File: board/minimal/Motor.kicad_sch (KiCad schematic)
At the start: 12 parts, among them IC1 DRV8835DSSR, J3 FR_ESC, J4 FL_ESC, J5 RMotor, J6 LMotor, J7 RR_ESC, J8 RL_ESC, Q1 DMP6050SSD

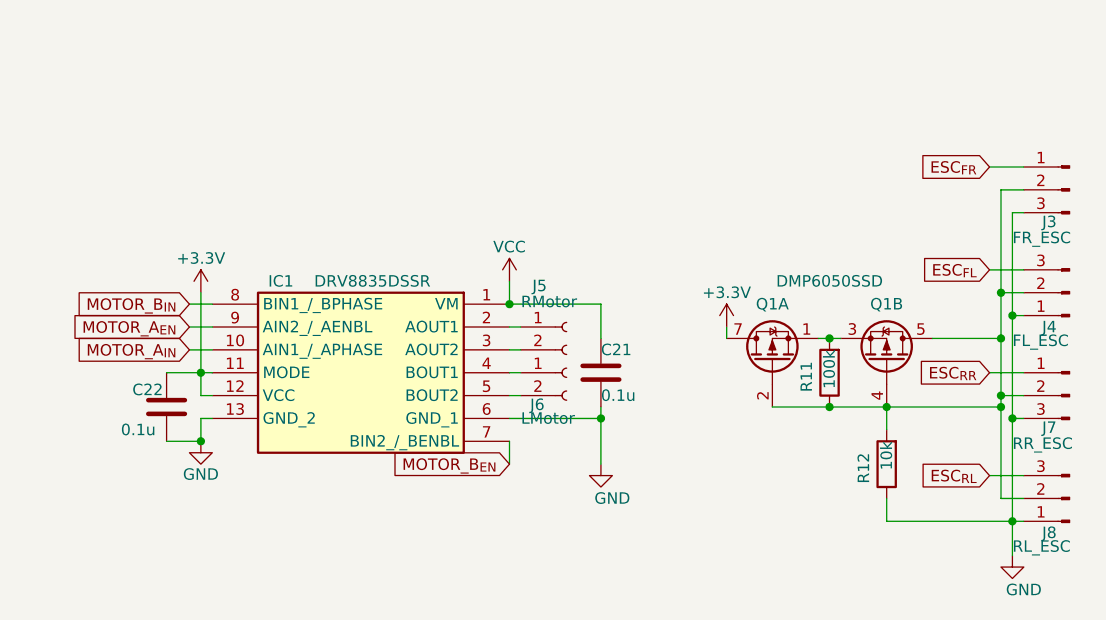
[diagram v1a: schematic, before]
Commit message: change core to rp2350b and some pin out
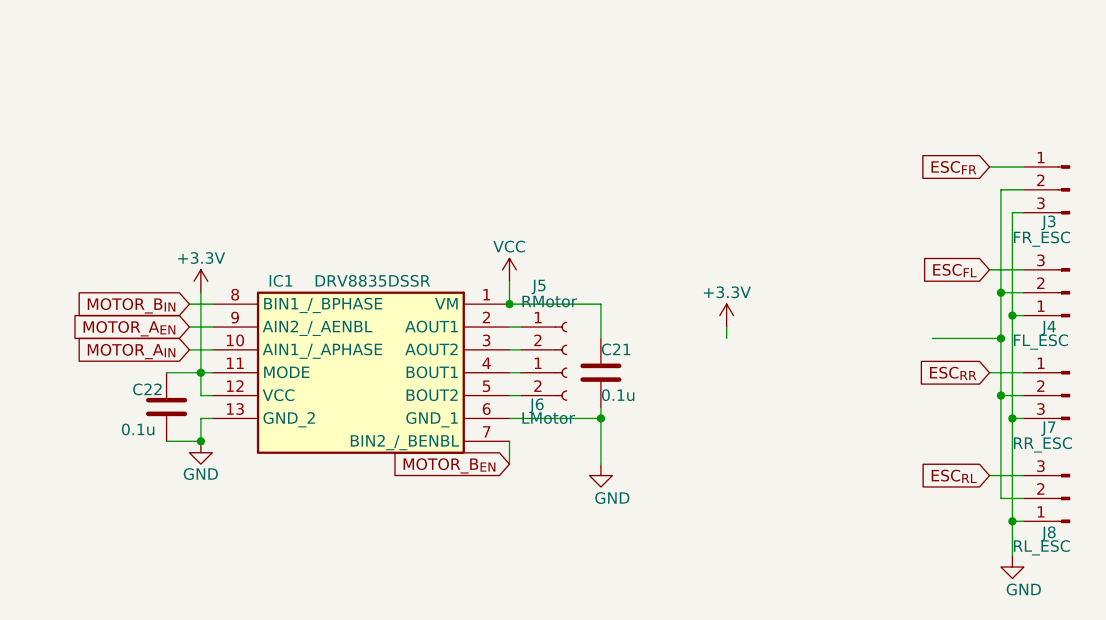
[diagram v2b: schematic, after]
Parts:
- removed Q1: DMP6050SSD, Package_SO:SOIC-8_3.9x4.9mm_P1.27mm, symbol Transistor_FET:DMP6050SSD
- removed R11: 100k, Resistor_SMD:R_0603_1608Metric, symbol Device:R
- removed R12: 10k, Resistor_SMD:R_0603_1608Metric, symbol Device:R

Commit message: add some connectors
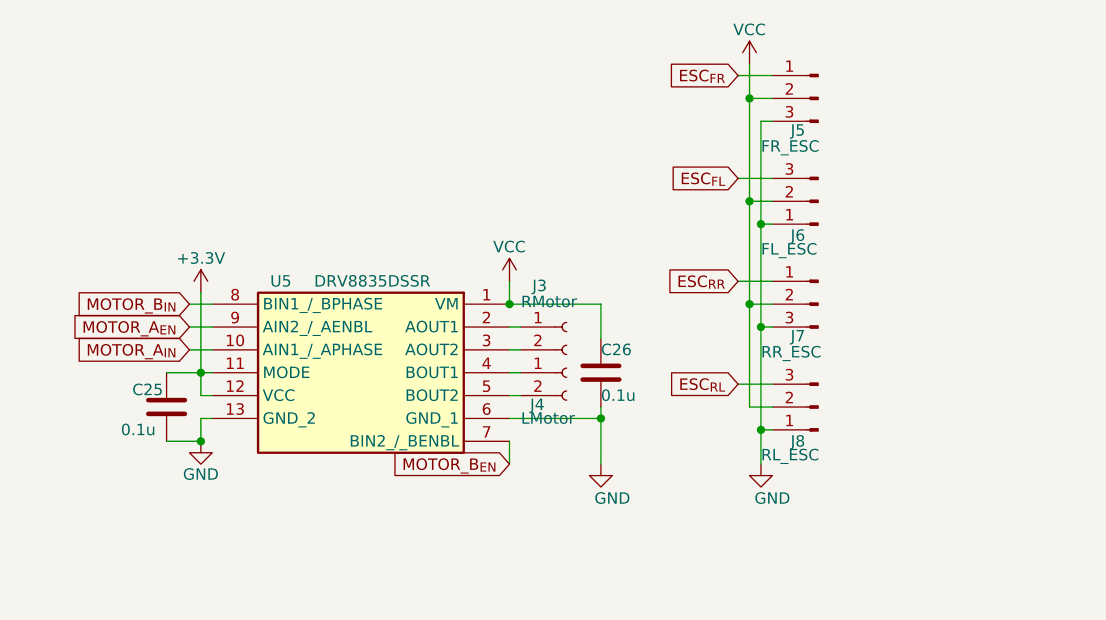
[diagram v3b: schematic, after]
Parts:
- renumbered C22 to C25, C21 to C26, J5 to J3, J6 to J4, J3 to J5, J4 to J6, IC1 to U5
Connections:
- net VCC: now also J5.2 (Pin_2), J6.2 (Pin_2), J7.2 (Pin_2), J8.2 (Pin_2)
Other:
- moved on the sheet: J5, J6, J7, J8

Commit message: set footprint
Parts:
- renumbered C25 to C26, C26 to C27, J3 to J4, J4 to J5, J5 to J6, J6 to J7, J7 to J8, J8 to J9
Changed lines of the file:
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@@
 		(on_board yes)
 		(dnp no)
-		(property "Reference" "#PWR032"
+		(property "Reference" "#PWR038"
 			(at 140.97 100.33 0)
 			(hide yes)
@@
 			(project "TurtlePico-Minimal"
 				(path "/7af2d99d-e350-48e7-86b4-20911ea922f3/30a58c44-3c8a-4ad6-a7be-85fee873ce7a"
-					(reference "#PWR032")
+					(reference "#PWR038")
 					(unit 1)
 				)
@@
 		(on_board yes)
 		(dnp no)
-		(property "Reference" "#PWR033"
+		(property "Reference" "#PWR039"
 			(at 151.13 123.19 0)
 			(hide yes)
@@
 			(project "TurtlePico-Minimal"
 				(path "/7af2d99d-e350-48e7-86b4-20911ea922f3/30a58c44-3c8a-4ad6-a7be-85fee873ce7a"
-					(reference "#PWR033")
+					(reference "#PWR039")
 					(unit 1)
 				)
@@
 		(on_board yes)
 		(dnp no)
-		(property "Reference" "#PWR031"
+		(property "Reference" "#PWR037"
 			(at 106.68 120.65 0)
 			(hide yes)
@@
 			(project "TurtlePico-Minimal"
 				(path "/7af2d99d-e350-48e7-86b4-20911ea922f3/30a58c44-3c8a-4ad6-a7be-85fee873ce7a"
-					(reference "#PWR031")
+					(reference "#PWR037")
 					(unit 1)
 				)
@@
 		(on_board yes)
 		(dnp no)
-		(property "Reference" "#PWR030"
+		(property "Reference" "#PWR036"
 			(at 106.68 101.6 0)
 			(hide yes)
@@
 			(project "TurtlePico-Minimal"
 				(path "/7af2d99d-e350-48e7-86b4-20911ea922f3/30a58c44-3c8a-4ad6-a7be-85fee873ce7a"
-					(reference "#PWR030")
+					(reference "#PWR036")
 					(unit 1)
 				)
@@
 		(on_board yes)
 		(dnp no)
-		(property "Reference" "C26"
+		(property "Reference" "C27"
 			(at 151.13 104.14 0)
 			(effects
@@
 			(project "TurtlePico-Minimal"
 				(path "/7af2d99d-e350-48e7-86b4-20911ea922f3/30a58c44-3c8a-4ad6-a7be-85fee873ce7a"
-					(reference "C26")
+					(reference "C27")
 					(unit 1)
 				)
@@
 		(on_board yes)
 		(dnp no)
-		(property "Reference" "C25"
+		(property "Reference" "C26"
 			(at 99.06 108.585 0)
 			(effects
@@
 			(project "TurtlePico-Minimal"
 				(path "/7af2d99d-e350-48e7-86b4-20911ea922f3/30a58c44-3c8a-4ad6-a7be-85fee873ce7a"
-					(reference "C25")
+					(reference "C26")
 					(unit 1)
 				)
@@
 		(on_board yes)
 		(dnp no)
-		(property "Reference" "J6"
+		(property "Reference" "J7"
 			(at 172.212 91.44 0)
 			(effects
@@
 			(project "TurtlePico-Minimal"
 				(path "/7af2d99d-e350-48e7-86b4-20911ea922f3/30a58c44-3c8a-4ad6-a7be-85fee873ce7a"
-					(reference "J6")
+					(reference "J7")
 					(unit 1)
 				)
@@
 		(on_board yes)
 		(dnp no)
-		(property "Reference" "#PWR035"
+		(property "Reference" "#PWR041"
 			(at 168.91 123.19 0)
 			(hide yes)
@@
 			(project "TurtlePico-Minimal"
 				(path "/7af2d99d-e350-48e7-86b4-20911ea922f3/30a58c44-3c8a-4ad6-a7be-85fee873ce7a"
-					(reference "#PWR035")
+					(reference "#PWR041")
 					(unit 1)
 				)
@@
 		(on_board yes)
 		(dnp no)
-		(property "Reference" "#PWR034"
+		(property "Reference" "#PWR040"
 			(at 167.64 76.2 0)
 			(hide yes)
@@
 			(project "TurtlePico-Minimal"
 				(path "/7af2d99d-e350-48e7-86b4-20911ea922f3/30a58c44-3c8a-4ad6-a7be-85fee873ce7a"
-					(reference "#PWR034")
+					(reference "#PWR040")
 					(unit 1)
 				)
@@
 		(on_board yes)
 		(dnp no)
-		(property "Reference" "J4"
+		(property "Reference" "J5"
 			(at 143.256 110.236 0)
 			(effects
@@
 			(project "TurtlePico-Minimal"
 				(path "/7af2d99d-e350-48e7-86b4-20911ea922f3/30a58c44-3c8a-4ad6-a7be-85fee873ce7a"
-					(reference "J4")
+					(reference "J5")
 					(unit 1)
 				)
@@
 		(on_board yes)
 		(dnp no)
-		(property "Reference" "J3"
+		(property "Reference" "J4"
 			(at 143.51 97.028 0)
 			(effects
@@
 			(project "TurtlePico-Minimal"
 				(path "/7af2d99d-e350-48e7-86b4-20911ea922f3/30a58c44-3c8a-4ad6-a7be-85fee873ce7a"
-					(reference "J3")
+					(reference "J4")
 					(unit 1)
 				)
@@
 		(on_board yes)
 		(dnp no)
-		(property "Reference" "J8"
+		(property "Reference" "J9"
 			(at 172.212 114.3 0)
 			(effects
@@
 			(project "TurtlePico-Minimal"
 				(path "/7af2d99d-e350-48e7-86b4-20911ea922f3/30a58c44-3c8a-4ad6-a7be-85fee873ce7a"
-					(reference "J8")
+					(reference "J9")
 					(unit 1)
 				)
@@
 		(on_board yes)
 		(dnp no)
-		(property "Reference" "J7"
+		(property "Reference" "J8"
 			(at 172.212 102.616 0)
 			(effects
@@
 			(project "TurtlePico-Minimal"
 				(path "/7af2d99d-e350-48e7-86b4-20911ea922f3/30a58c44-3c8a-4ad6-a7be-85fee873ce7a"
-					(reference "J7")
+					(reference "J8")
 					(unit 1)
 				)
@@
 		(on_board yes)
 		(dnp no)
-		(property "Reference" "J5"
+		(property "Reference" "J6"
 			(at 172.212 79.756 0)
 			(effects
@@
 			(project "TurtlePico-Minimal"
 				(path "/7af2d99d-e350-48e7-86b4-20911ea922f3/30a58c44-3c8a-4ad6-a7be-85fee873ce7a"
-					(reference "J5")
-					(unit 1)
-				)
+					(reference "J6")
+					(unit 1)
+				)
